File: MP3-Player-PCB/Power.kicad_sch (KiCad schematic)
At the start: 44 parts, among them J201 Conn_01x02_Socket, J202 USB_C_Receptacle_USB2.0_16P, U201 BQ24259, U202 USBLC6-2SC6, U203 TPS7A2033PDBVR, U204 TPS7A2033PDBVR

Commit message: Replaced JST connector with picoblade to match purchased battery
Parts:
- J201: footprint Connector_JST:JST_GH_SM02B-GHS-TB_1x02-1MP_P1.25mm_Horizontal -> Connector_Molex:Molex_PicoBlade_53048-0210_1x02_P1.25mm_Horizontal
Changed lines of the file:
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@@
 			)
 		)
-		(property "Footprint" "Connector_JST:JST_GH_SM02B-GHS-TB_1x02-1MP_P1.25mm_Horizontal"
+		(property "Footprint" "Connector_Molex:Molex_PicoBlade_53048-0210_1x02_P1.25mm_Horizontal"
 			(at 248.92 49.53 0)
 			(effects

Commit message: Added JLCPCB part numbers for remaining parts
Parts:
- R207: value 5.25k -> 5.23k; JLCPCB Part # (none) -> C25907
- R208: value 317R -> 316R; JLCPCB Part # (none) -> C247119
- R217: value 10k -> 31.6k; JLCPCB Part # C25744 -> C11463
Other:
- note removed: "Make sure to get polarity correct!"
- note removed: "Make sure to pick NTC and dependent resistor!"
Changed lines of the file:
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@@
 		)
 	)
-	(text "Make sure to pick NTC and dependent resistor!\n"
-		(exclude_from_sim no)
-		(at 194.056 84.836 0)
-		(effects
-			(font
-				(size 1.27 1.27)
-			)
-		)
-	)
-	(text "Make sure to get polarity correct!"
-		(exclude_from_sim no)
-		(at 281.178 56.388 0)
-		(effects
-			(font
-				(size 2.54 2.54)
-				(thickness 0.254)
-				(bold yes)
-			)
-		)
-	)
 	(text "Set ILIM via register"
 		(exclude_from_sim no)
@@
 			)
 		)
-		(property "Value" "10k"
+		(property "Value" "31.6k"
 			(at 209.55 71.1199 0)
 			(effects
@@
 			)
 		)
-		(property "JLCPCB Part #" "C25744"
+		(property "JLCPCB Part #" "C11463"
 			(at 207.01 69.85 0)
 			(effects
@@
 			)
 		)
-		(property "Value" "5.25k"
+		(property "Value" "5.23k"
 			(at 203.2 60.9599 0)
 			(effects
@@
 			)
 		)
-		(property "JLCPCB Part #" ""
+		(property "JLCPCB Part #" "C25907"
 			(at 200.66 59.69 0)
 			(effects
@@
 			)
 		)
-		(property "Value" "317R"
+		(property "Value" "316R"
 			(at 180.34 71.1199 0)
 			(effects
@@
 			)
 		)
-		(property "JLCPCB Part #" ""
+		(property "JLCPCB Part #" "C247119"
 			(at 177.8 69.85 0)
 			(effects

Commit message: Ordered MP3 Playergit status! Finally :)
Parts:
- J201: JLCPCB Part # C189893 -> C505099
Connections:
- net +VBAT: now also R214.1
- net +VSYS: no longer R214.1
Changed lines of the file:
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@@
+	)
+	(symbol
+		(lib_id "power:VBUS")
+		(at 234.95 83.82 0)
+		(unit 1)
+		(exclude_from_sim no)
+		(in_bom yes)
+		(on_board yes)
+		(dnp no)
+		(property "Reference" "#PWR01"
+			(at 234.95 87.63 0)
+			(effects
+				(font
+					(size 1.27 1.27)
+				)
+				(hide yes)
+			)
+		)
+		(property "Value" "+VBAT"
+			(at 234.95 80.01 0)
+			(effects
+				(font
+					(size 1.27 1.27)
+				)
+			)
+		)
+		(property "Footprint" ""
+			(at 234.95 83.82 0)
+			(effects
+				(font
+					(size 1.27 1.27)
+				)
+				(hide yes)
+			)
+		)
+		(property "Datasheet" ""
+			(at 234.95 83.82 0)
+			(effects
+				(font
+					(size 1.27 1.27)
+				)
+				(hide yes)
+			)
+		)
+		(property "Description" "Power symbol creates a global label with name \"VBUS\""
+			(at 234.95 83.82 0)
+			(effects
+				(font
+					(size 1.27 1.27)
+				)
+				(hide yes)
+			)
+		)
+		(pin "1"
+		)
+		(instances
+			(project "MP3-Player"
+				(path "/3f51ea9b-d2e1-4711-a47c-269e1b97e0f4/156723cf-95cb-4e74-b8dc-320a10f9d20f"
+					(reference "#PWR01")
+					(unit 1)
+				)
+			)
+		)
 	)
 	(symbol
@@
 			)
 		)
-		(property "JLCPCB Part #" "C189893"
+		(property "JLCPCB Part #" "C505099"
 			(at 248.92 49.53 0)
 			(effects
@@
 					(unit 1)
 				)
-			)
-		)
-	)
-	(symbol
-		(lib_id "power:VBUS")
-		(at 234.95 83.82 0)
-		(unit 1)
-		(exclude_from_sim no)
-		(in_bom yes)
-		(on_board yes)
-		(dnp no)
-		(fields_autoplaced yes)
-		(property "Reference" "#PWR0221"
-			(at 234.95 87.63 0)
-			(effects
-				(font
-					(size 1.27 1.27)
-				)
-				(hide yes)
-			)
-		)
-		(property "Value" "+VSYS"
-			(at 234.95 78.74 0)
-			(effects
-				(font
-					(size 1.27 1.27)
-				)
-			)
-		)
-		(property "Footprint" ""
-			(at 234.95 83.82 0)
-			(effects
-				(font
-					(size 1.27 1.27)
-				)
-				(hide yes)
-			)
-		)
-		(property "Datasheet" ""
-			(at 234.95 83.82 0)
-			(effects
-				(font
-					(size 1.27 1.27)
-				)
-				(hide yes)
-			)
-		)
-		(property "Description" "Power symbol creates a global label with name \"VBUS\""
-			(at 234.95 83.82 0)
-			(effects
-				(font
-					(size 1.27 1.27)
-				)
-				(hide yes)
-			)
-		)
-		(pin "1"
-		)
-		(instances
-			(project "MP3-Player"
-				(path "/3f51ea9b-d2e1-4711-a47c-269e1b97e0f4/156723cf-95cb-4e74-b8dc-320a10f9d20f"
-					(reference "#PWR0221")
-					(unit 1)
-				)

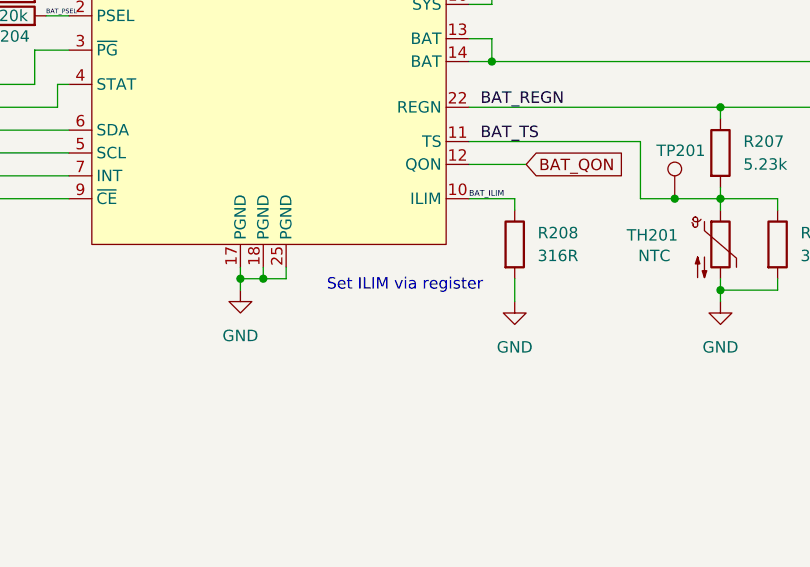
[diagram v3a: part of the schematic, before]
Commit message: Added CubeMX timer PWM stock code
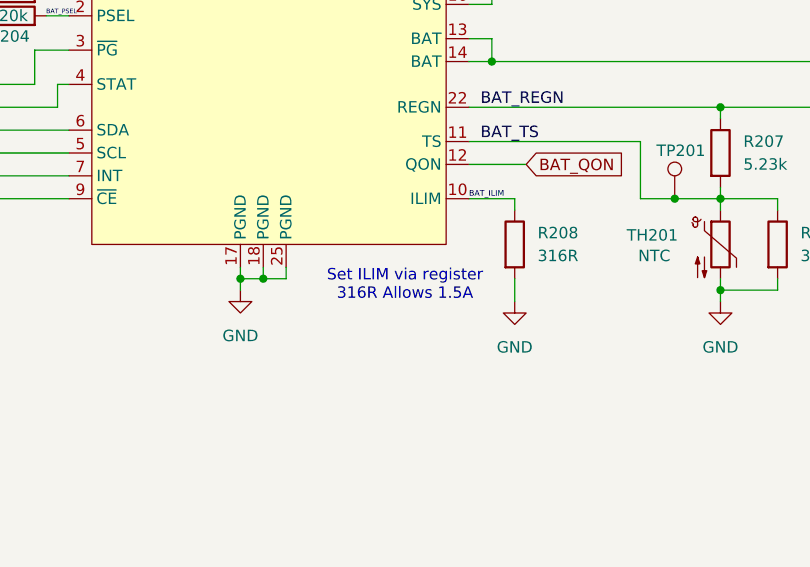
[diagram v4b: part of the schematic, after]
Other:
- note added: "Set ILIM via register 316R Allows 1.5A"
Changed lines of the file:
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@@
 		)
 	)
-	(text "Set ILIM via register"
+	(text "Set ILIM via register\n316R Allows 1.5A"
 		(exclude_from_sim no)
 		(at 165.608 74.422 0)
